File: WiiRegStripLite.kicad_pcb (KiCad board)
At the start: 2 copper layers, 55.5 x 55 mm, 74 parts, among them J1 Conn_01x04_Socket, J2 Conn_01x04_Socket, J3 Fan, U10 TLV62585DRL, U11 TPS61023DRLR, U5 BQ25895RTW, U6 ATtiny1616-M, U7 TLV62585DRL, U8 TLV62585DRL, U9 TLV62585DRL

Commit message: Some more work
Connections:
- R27 pad 2: 3V -> VIN
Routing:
- net 3V: track 72.8 -> 37.0 mm, vias 4 -> 2
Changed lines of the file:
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@@
 			(at 0 -1.448 0)
 			(layer "F.SilkS")
+			(hide yes)
 			(effects
 				(font
@@
 			(at 0 1.55 0)
 			(layer "F.Fab")
+			(hide yes)
 			(effects
 				(font
@@
 			(layer "F.CrtYd")
 		)
-		(fp_text user "${REFERENCE}"
-			(at 0 -1.45 0)
-			(layer "F.Fab")
-			(effects
-				(font
-					(size 1 1)
-					(thickness 0.15)
-				)
-			)
-		)
 		(pad "1" smd circle
 			(at 0 0)
@@
 			(layers "F.Cu" "F.Paste" "F.Mask")
 			(roundrect_rratio 0.25)
-			(net 5 "3V")
+			(net 3 "VIN")
 			(pintype "passive")
 		)
@@
 	)
 	(segment
-		(start 173.91 133.31)
-		(end 175.08 133.31)
-		(width 0.2)
-		(layer "F.Cu")
-		(net 5)
-	)
-	(segment
 		(start 181.88 123.31)
 		(end 182.25 122.94)
@@
 	)
 	(segment
-		(start 175.08 133.31)
-		(end 177.17 131.22)
-		(width 0.2)
-		(layer "F.Cu")
-		(net 5)
-	)
-	(segment
 		(start 186.61 112.1)
 		(end 186.92 112.1)
@@
 	)
 	(segment
-		(start 149.339101 137.37204)
-		(end 153.16204 137.37204)
-		(width 0.2)
-		(layer "F.Cu")
-		(net 5)
-	)
-	(segment
 		(start 182.25 122.94)
 		(end 182.25 114.23)
@@
 	)
 	(segment
-		(start 153.16204 137.37204)
-		(end 154.31 138.52)
-		(width 0.2)
-		(layer "F.Cu")
-		(net 5)
-	)
-	(segment
 		(start 182.69 113.79)
 		(end 184.92 113.79)
@@
 	)
 	(segment
-		(start 173.91 133.31)
-		(end 173.92 133.31)
-		(width 0.2)
-		(layer "F.Cu")
-		(net 5)
-	)
-	(segment
 		(start 179.758 124.263192)
 		(end 180.926808 124.263192)
@@
 	)
 	(via
-		(at 173.91 133.31)
-		(size 0.6)
-		(drill 0.3)
-		(layers "F.Cu" "B.Cu")
-		(net 5)
-	)
-	(via
 		(at 187.1 112.1)
 		(size 0.6)
@@
 		(net 5)
 	)
-	(via
-		(at 149.339101 137.37204)
-		(size 0.6)
-		(drill 0.3)
-		(layers "F.Cu" "B.Cu")
-		(net 5)
-	)
-	(segment
-		(start 149.339101 137.37204)
-		(end 153.401141 133.31)
-		(width 0.2)
-		(layer "B.Cu")
-		(net 5)
-	)
 	(segment
 		(start 187.1 112.1)
@@
 		(width 0.2)
 		(layer "B.Cu")
-		(net 5)
-	)
-	(segment
-		(start 153.401141 133.31)
-		(end 154.44 133.31)
-		(width 0.2)
-		(layer "B.Cu")
-		(net 5)
-	)
-	(segment
-		(start 154.44 133.31)
-		(end 173.91 133.31)
-		(width 0.2)
-		(layer "B.Cu")

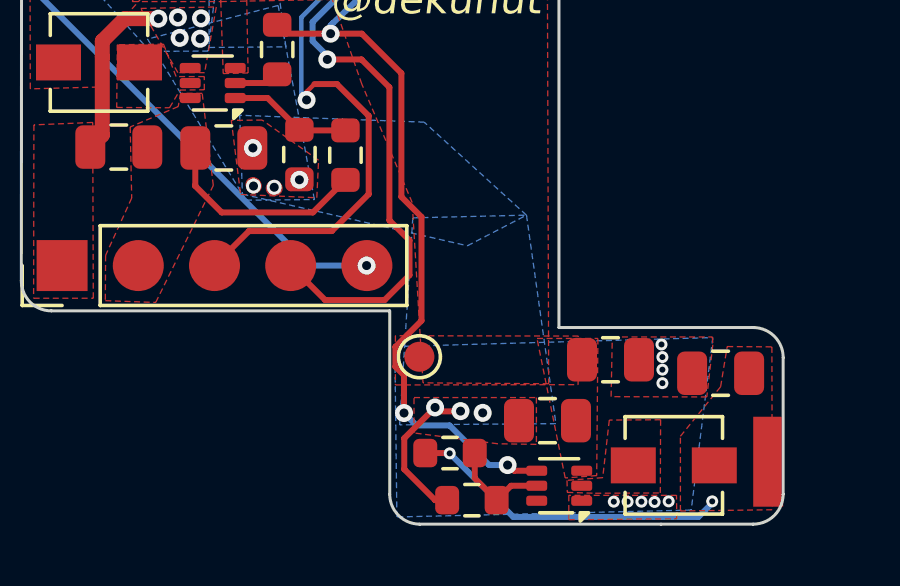
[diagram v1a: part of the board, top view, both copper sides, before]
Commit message: Added U10 emulation on TX Pad of pcb
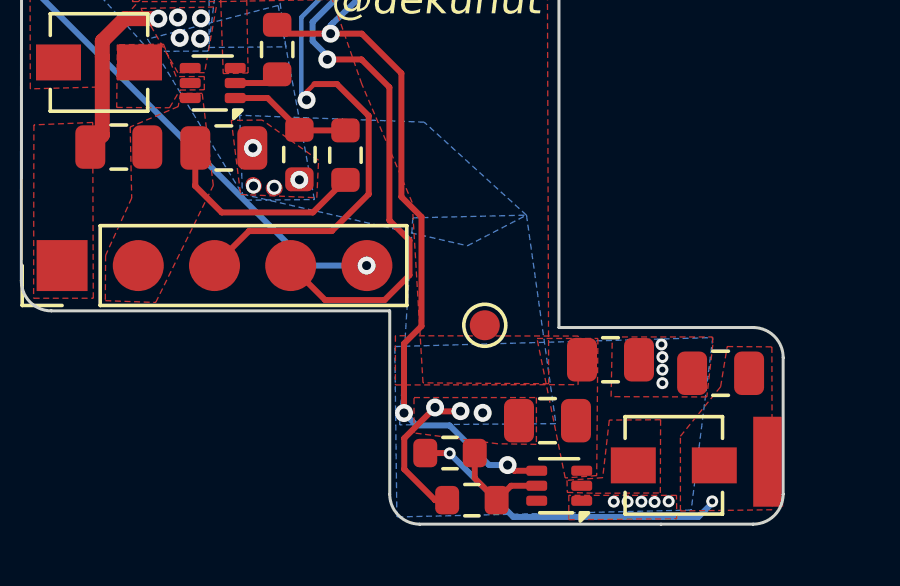
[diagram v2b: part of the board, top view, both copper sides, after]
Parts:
- moved TP3 2.42 mm to (152.7, 151.8)
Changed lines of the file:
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@@
 	(footprint "TestPoint:TestPoint_Pad_D1.0mm"
 		(layer "F.Cu")
-		(at 150.49 152.86)
+		(at 152.67 151.81)
 		(descr "SMD pad as test Point, diameter 1.0mm")
 		(tags "test point SMD pad")
@@
 	)
 	(segment
-		(start 184.2 120.2)
-		(end 183.61 120.79)
+		(start 149.977333 152.422667)
+		(end 150.56 151.84)
 		(width 0.2)
 		(layer "F.Cu")
@@
 	)
 	(segment
-		(start 148.57 142.09)
-		(end 147.53 142.09)
+		(start 184.2 120.2)
+		(end 183.61 120.79)
 		(width 0.2)
 		(layer "F.Cu")
@@
 	)
 	(segment
-		(start 149.89 143.41)
-		(end 148.57 142.09)
+		(start 147.95 139.02)
+		(end 150.45 139.02)
 		(width 0.2)
 		(layer "F.Cu")
@@
 	)
 	(segment
-		(start 149.977333 153.478704)
-		(end 149.69 153.191371)
+		(start 185.5 126.5925)
+		(end 185.5 127.26)
 		(width 0.2)
 		(layer "F.Cu")
@@
 	)
 	(segment
-		(start 147.95 139.02)
-		(end 150.45 139.02)
+		(start 150.56 148.2)
+		(end 149.89 147.53)
 		(width 0.2)
 		(layer "F.Cu")
@@
 	)
 	(segment
-		(start 185.5 126.5925)
-		(end 185.5 127.26)
+		(start 148.57 142.09)
+		(end 147.53 142.09)
 		(width 0.2)
 		(layer "F.Cu")
@@
 	)
 	(segment
-		(start 150.56 151.658629)
-		(end 150.56 148.2)
+		(start 149.977333 154.735861)
+		(end 149.977333 152.422667)
+		(width 0.2)
+		(layer "F.Cu")
+		(net 26)
+	)
+	(segment
+		(start 149.89 143.41)
+		(end 148.57 142.09)
 		(width 0.2)
 		(layer "F.Cu")
@@
 	)
 	(segment
-		(start 149.977333 154.735861)
-		(end 149.977333 153.478704)
-		(width 0.2)
-		(layer "F.Cu")
-		(net 26)
-	)
-	(segment
 		(start 185.22 123.96)
 		(end 185.2 123.97)
@@
 	)
 	(segment
-		(start 150.56 148.2)
-		(end 149.89 147.53)
-		(width 0.2)
-		(layer "F.Cu")
-		(net 26)
-	)
-	(segment
 		(start 153.65 156.66)
 		(end 153.46 156.47)
@@
 	)
 	(segment
-		(start 149.89 147.53)
-		(end 149.89 143.41)
-		(width 0.2)
-		(layer "F.Cu")
-		(net 26)
-	)
-	(segment
-		(start 149.69 153.191371)
-		(end 149.69 152.528629)
+		(start 174.965 141.11)
+		(end 177.72 141.11)
 		(width 0.2)
 		(layer "F.Cu")
@@
 	)
 	(segment
-		(start 174.965 141.11)
-		(end 177.72 141.11)
+		(start 149.89 147.53)
+		(end 149.89 143.41)
 		(width 0.2)
 		(layer "F.Cu")
@@
 	)
 	(segment
-		(start 149.69 152.528629)
-		(end 150.56 151.658629)
+		(start 150.56 151.84)
+		(end 150.56 148.2)
 		(width 0.2)
 		(layer "F.Cu")
